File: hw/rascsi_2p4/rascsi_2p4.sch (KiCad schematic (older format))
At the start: 89 parts, among them IC1 SN74LS641-1DW, IC2 SN74LS641-1DW, IC3 SN74LS641-1DW, IC4 SN74LS641-1DW, J1 Raspberry_Pi_2_3, J2 DNP, J4 I2C Pinout, J5 DNP, J6 CONNFLY DB-25, J7 DNP, X1 Mac, X2 Dogcow, X3 Mac, X4 Dogcow, X5 Dogcow, X6 Dogcow, X7 Pi, X8 Pi

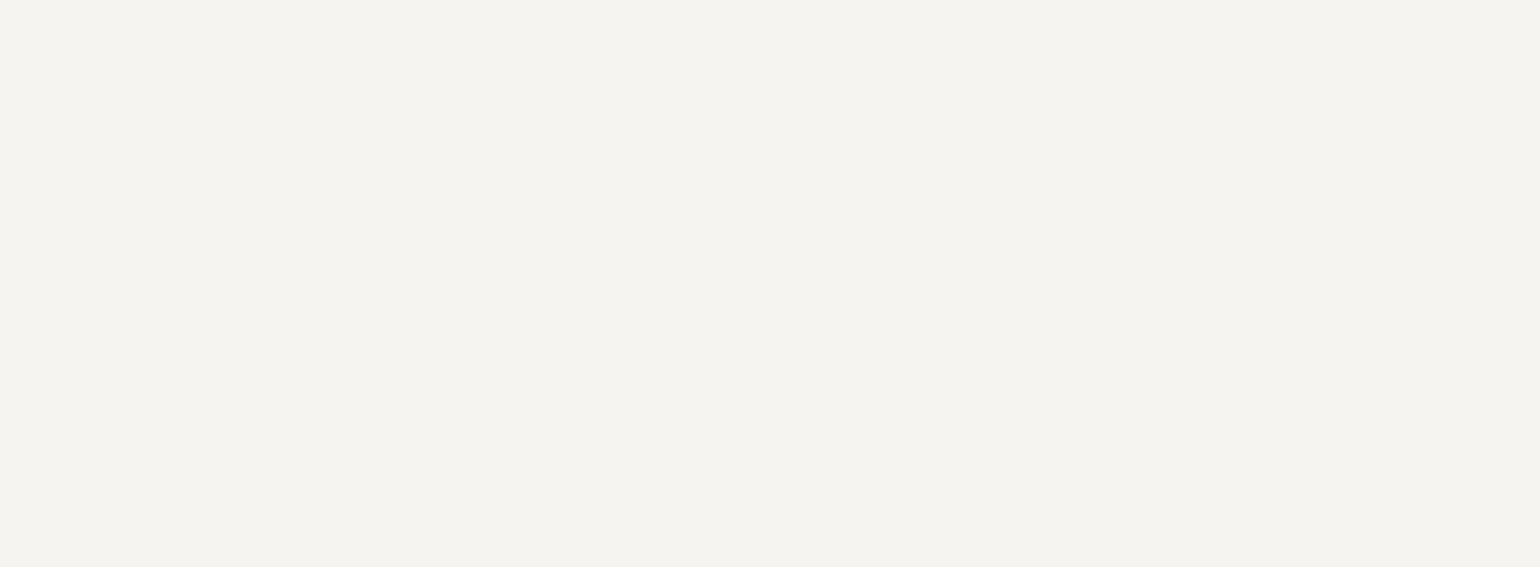
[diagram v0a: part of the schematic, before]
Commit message: replaced 4x74LS641 by 2x74ALVC164245DGG added pulldowns for floating in/out pins (instead of directly wiring them to ground) setup for autorouting
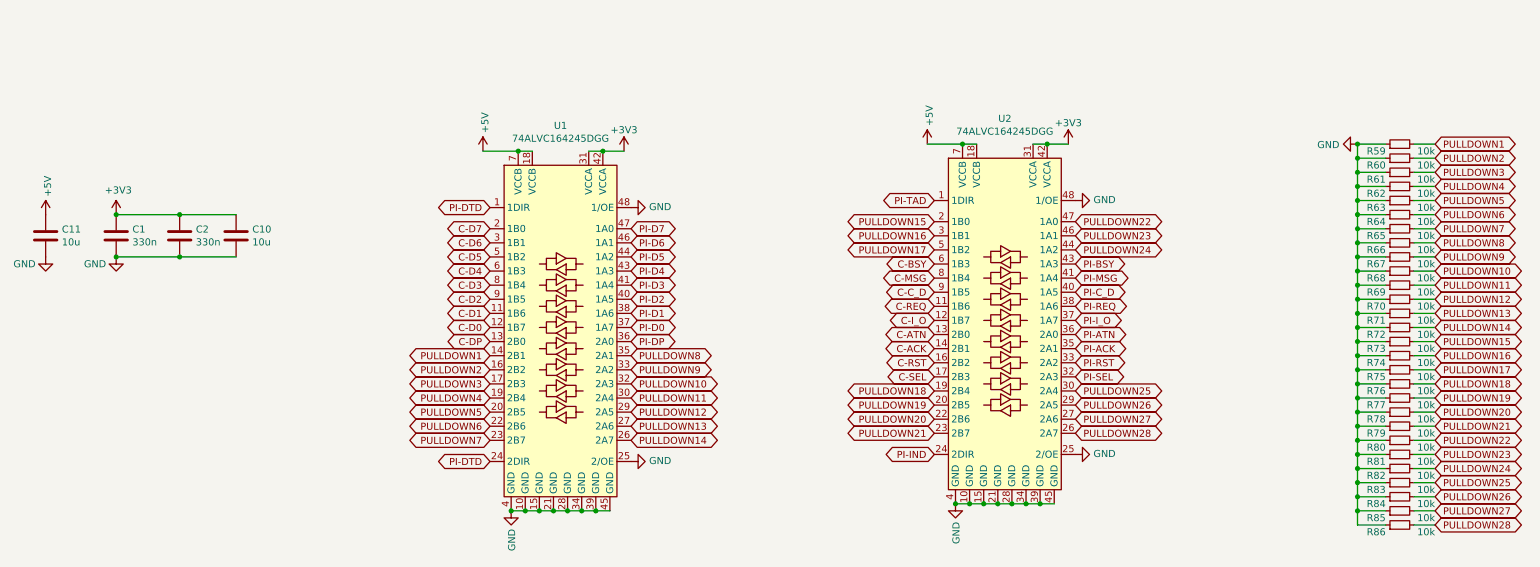
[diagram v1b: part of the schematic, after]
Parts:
- added C1, C2: 330n, Capacitor_SMD:C_0805_2012Metric, symbol Device:C
- added C10, C11: 10u, Capacitor_SMD:C_0805_2012Metric, symbol Device:C
- added R59, R60, R61, R62, R63, R64, R65, R66, R67, R68, R69, R70, R71, R72, R73, R74, R75, R76, R77, R78, R79, R80, R81, R82, R83, R84, R85, R86: 10k, Resistor_SMD:R_0402_1005Metric, symbol Device:R_Small
- added U1, U2: 74ALVC164245DGG, Package_SO:TSSOP-48_6.1x12.5mm_P0.5mm, symbol amiga:74ALVC164245DGG
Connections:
- net +3V3: now also C1.1, C10.1, C2.1, U1.31 (VCCA), U1.42 (VCCA), U2.31 (VCCA), U2.42 (VCCA)
- net +5V: now also C11.1, U1.18 (VCCB), U1.7 (VCCB), U2.18 (VCCB), U2.7 (VCCB)
- net C-ACK: now also U2.14 (2B1)
- net C-ATN: now also U2.13 (2B0)
- net C-BSY: now also U2.6 (1B3)
- net C-C_D: now also U2.9 (1B5)
- net C-D0: now also U1.12 (1B7)
- net C-D1: now also U1.11 (1B6)
- net C-D2: now also U1.9 (1B5)
- net C-D3: now also U1.8 (1B4)
- net C-D4: now also U1.6 (1B3)
- net C-D5: now also U1.5 (1B2)
- net C-D6: now also U1.3 (1B1)
- net C-D7: now also U1.2 (1B0)
- net C-DP: now also U1.13 (2B0)
- net C-I_O: now also U2.12 (1B7)
- net C-MSG: now also U2.8 (1B4)
- net C-REQ: now also U2.11 (1B6)
- net C-RST: now also U2.16 (2B2)
- net C-SEL: now also U2.17 (2B3)
- net GND: now also C1.2, C10.2, C11.2, C2.2, R59.1, R60.1, R61.1, R62.1, R63.1, R64.1, R65.1, R66.1, R67.1, R68.1, R69.1, R70.1, R71.1, R72.1, R73.1, R74.1, R75.1, R76.1, R77.1, R78.1, R79.1, R80.1, R81.1, R82.1, R83.1, R84.1, R85.1, R86.1, U1.10 (GND), U1.15 (GND), U1.21 (GND), U1.25 (2/OE), U1.28 (GND), U1.34 (GND), U1.39 (GND), U1.4 (GND), U1.45 (GND), U1.48 (1/OE), U2.10 (GND), U2.15 (GND), U2.21 (GND), U2.25 (2/OE), U2.28 (GND), U2.34 (GND), U2.39 (GND), U2.4 (GND), U2.45 (GND), U2.48 (1/OE)
- net PI-ACK: now also U2.35 (2A1)
- net PI-ATN: now also U2.36 (2A0)
- net PI-BSY: now also U2.43 (1A3)
- net PI-C_D: now also U2.40 (1A5)
- net PI-D0: now also U1.37 (1A7)
- net PI-D1: now also U1.38 (1A6)
- net PI-D2: now also U1.40 (1A5)
- net PI-D3: now also U1.41 (1A4)
- net PI-D4: now also U1.43 (1A3)
- net PI-D5: now also U1.44 (1A2)
- net PI-D6: now also U1.46 (1A1)
- net PI-D7: now also U1.47 (1A0)
- net PI-DP: now also U1.36 (2A0)
- net PI-DTD: now also U1.1 (1DIR), U1.24 (2DIR)
- net PI-IND: now also U2.24 (2DIR)
- net PI-I_O: now also U2.37 (1A7)
- net PI-MSG: now also U2.41 (1A4)
- net PI-REQ: now also U2.38 (1A6)
- net PI-RST: now also U2.33 (2A2)
- net PI-SEL: now also U2.32 (2A3)
- net PI-TAD: now also U2.1 (1DIR)
- new net PULLDOWN1: R59.2, U1.14 (2B1)
- new net PULLDOWN10: R68.2, U1.32 (2A3)
- new net PULLDOWN11: R69.2, U1.30 (2A4)
- new net PULLDOWN12: R70.2, U1.29 (2A5)
- new net PULLDOWN13: R71.2, U1.27 (2A6)
- new net PULLDOWN14: R72.2, U1.26 (2A7)
- new net PULLDOWN15: R73.2, U2.2 (1B0)
- new net PULLDOWN16: R74.2, U2.3 (1B1)
- new net PULLDOWN17: R75.2, U2.5 (1B2)
- new net PULLDOWN18: R76.2, U2.19 (2B4)
- new net PULLDOWN19: R77.2, U2.20 (2B5)
- new net PULLDOWN2: R60.2, U1.16 (2B2)
- new net PULLDOWN20: R78.2, U2.22 (2B6)
- new net PULLDOWN21: R79.2, U2.23 (2B7)
- new net PULLDOWN22: R80.2, U2.47 (1A0)
- new net PULLDOWN23: R81.2, U2.46 (1A1)
- new net PULLDOWN24: R82.2, U2.44 (1A2)
- new net PULLDOWN25: R83.2, U2.30 (2A4)
- new net PULLDOWN26: R84.2, U2.29 (2A5)
- new net PULLDOWN27: R85.2, U2.27 (2A6)
- new net PULLDOWN28: R86.2, U2.26 (2A7)
- new net PULLDOWN3: R61.2, U1.17 (2B3)
- new net PULLDOWN4: R62.2, U1.19 (2B4)
- new net PULLDOWN5: R63.2, U1.20 (2B5)
- new net PULLDOWN6: R64.2, U1.22 (2B6)
- new net PULLDOWN7: R65.2, U1.23 (2B7)
- new net PULLDOWN8: R66.2, U1.35 (2A1)
- new net PULLDOWN9: R67.2, U1.33 (2A2)
